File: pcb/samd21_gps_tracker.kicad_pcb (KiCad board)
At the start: 4 copper layers, 99 x 38.5 mm, 95 parts, among them J1 JTAG_SWD_6, J2 01x04, J3 U.FL-R-SMT, J4 SIM_Card, J5 USB_C_Receptacle_USB2.0, J6 U.FL-R-SMT, J7 C7244, Q1 2N7002, Q2 2N7002, Q3 2N7002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

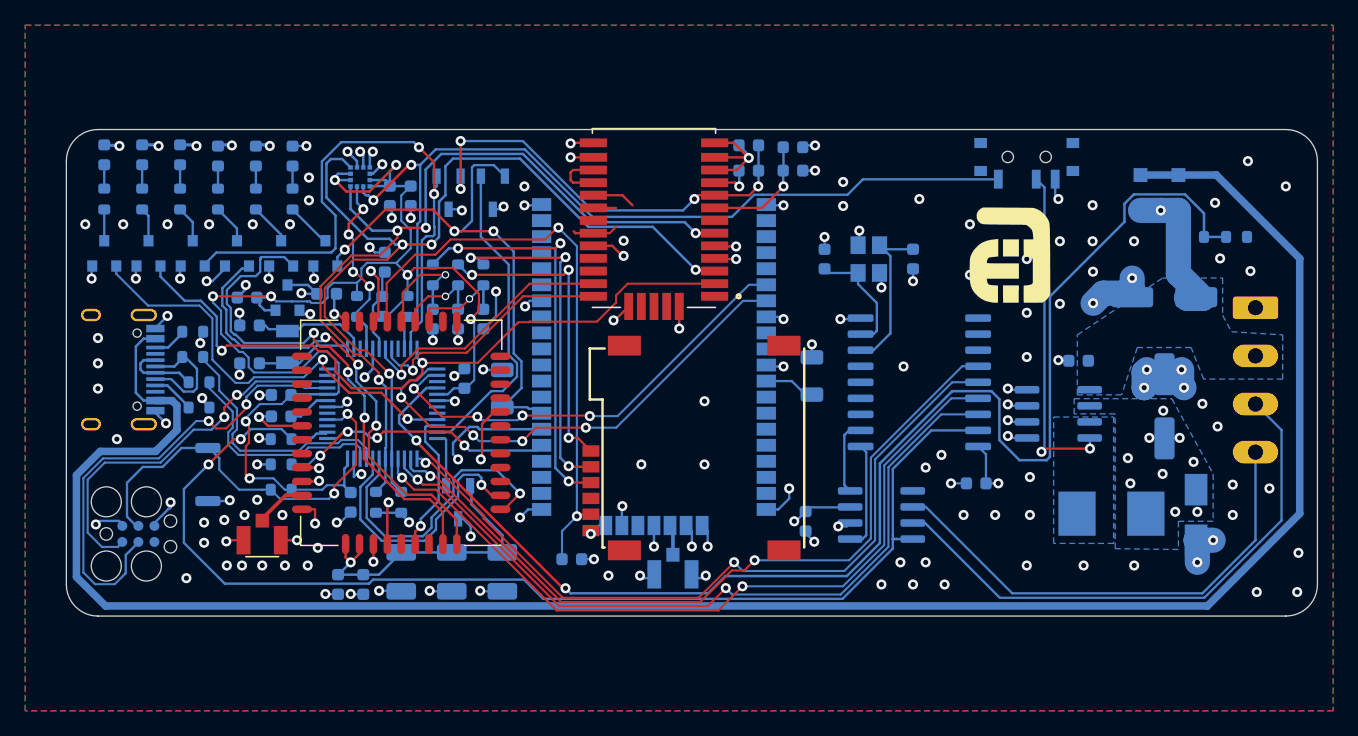
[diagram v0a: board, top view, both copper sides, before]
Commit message: REV 1 - WIP
Fixed D3, it was the wrong way around
Fixed Q6, Q7, Q8, D and S were the wrong way around
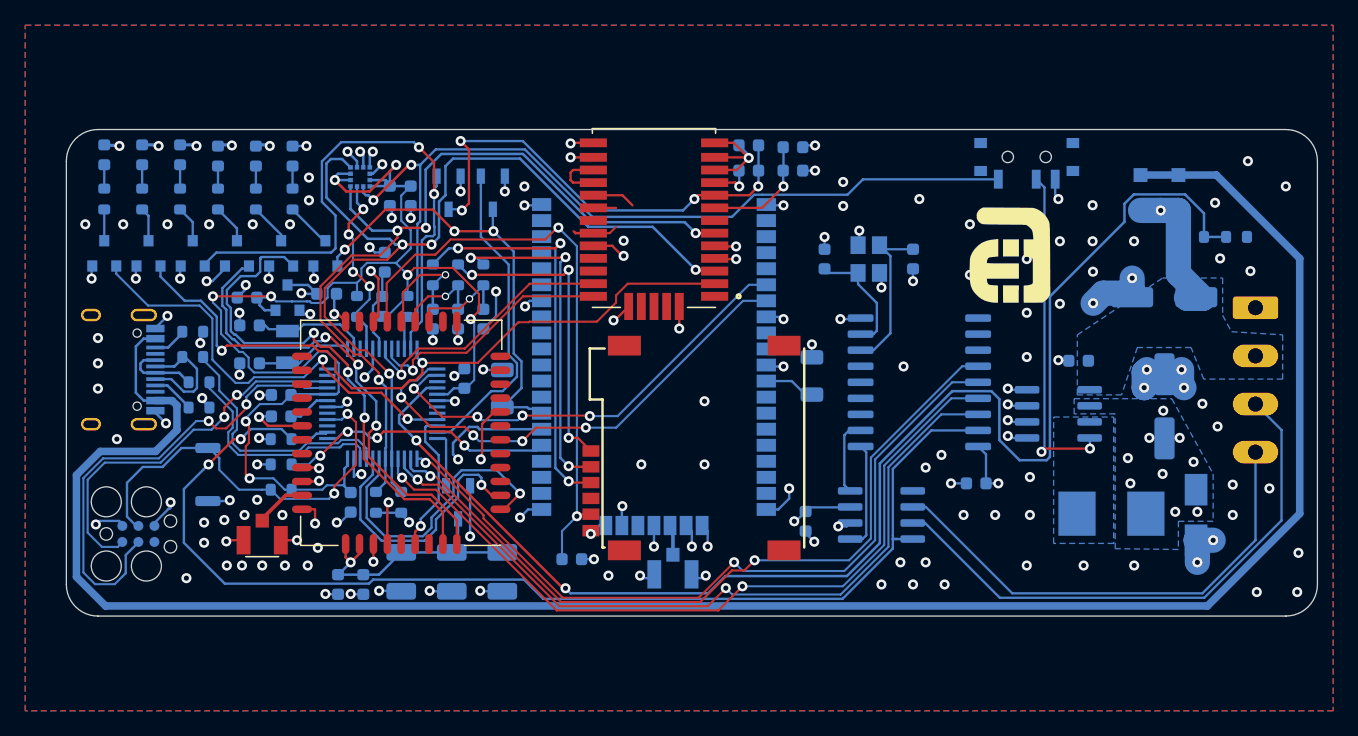
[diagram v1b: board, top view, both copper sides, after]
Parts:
- turned D3 to 270 degrees
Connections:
- D3 pad 1: GND -> +3V3
- D3 pad 2: +3V3 -> GND
- Q6 pad 2: LoRa_VCC -> +3V3
- Q6 pad 3: +3V3 -> LoRa_VCC
- Q7 pad 2: Net-(C15-Pad1) -> +3V3
- Q7 pad 3: +3V3 -> Net-(C15-Pad1)
- Q8 pad 2: Net-(C26-Pad1) -> +3V3
- Q8 pad 3: +3V3 -> Net-(C26-Pad1)
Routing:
- net LoRa_VCC: track 47.5 -> 40.2 mm
- net Net-(C26-Pad1): track 24.7 -> 21.0 mm
- net +3V3: track 37.4 -> 39.8 mm
- net Net-(C15-Pad1): track 34.7 -> 37.0 mm
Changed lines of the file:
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@@
     (thickness 1.6)
     (drawings 18)
-    (tracks 1464)
+    (tracks 1456)
     (zones 0)
     (modules 95)
@@
   )
   (setup
-    (last_trace_width 0.167)
+    (last_trace_width 0.187)
     (user_trace_width 0.187)
     (user_trace_width 0.2)
@@
   )
   (module Diode_SMD:D_SMA (layer B.Cu)
-    (at 227.9 68 90)
+    (at 227.9 68 270)
     (descr "Diode SMA (DO-214AC)")
     (tags "Diode SMA (DO-214AC)")
@@
       (effects (font (size 1 1) (thickness 0.15)) (justify mirror))
     )
-    (pad 1 smd rect (at -2 0 90) (size 2.5 1.8) (layers B.Cu B.Paste B.Mask)
-      (net 1 GND))
-    (pad 2 smd rect (at 2 0 90) (size 2.5 1.8) (layers B.Cu B.Paste B.Mask)
+    (pad 1 smd rect (at -2 0 270) (size 2.5 1.8) (layers B.Cu B.Paste B.Mask)
       (net 4 +3V3))
+    (pad 2 smd rect (at 2 0 270) (size 2.5 1.8) (layers B.Cu B.Paste B.Mask)
+      (net 1 GND))
     (model ${KISYS3DMOD}/Diode_SMD.3dshapes/D_SMA.wrl
       (at (xyz 0 0 0))
@@
     )
     (pad 3 smd rect (at 1.31 0 270) (size 1.22 0.65) (layers B.Cu B.Paste B.Mask)
-      (net 4 +3V3))
-    (pad 2 smd rect (at -1.31 -0.95 270) (size 1.22 0.65) (layers B.Cu B.Paste B.Mask)
       (net 10 LoRa_VCC))
+    (pad 2 smd rect (at -1.31 -0.95 270) (size 1.22 0.65) (layers B.Cu B.Paste B.Mask)
+      (net 4 +3V3))
     (pad 1 smd rect (at -1.31 0.95 270) (size 1.22 0.65) (layers B.Cu B.Paste B.Mask)
       (net 42 LoRa_ON))
@@
       (net 39 GPS_ON))
     (pad 2 smd rect (at -1.31 -0.95 270) (size 1.22 0.65) (layers B.Cu B.Paste B.Mask)
-      (net 11 "Net-(C15-Pad1)"))
-    (pad 3 smd rect (at 1.31 0 270) (size 1.22 0.65) (layers B.Cu B.Paste B.Mask)
       (net 4 +3V3))
+    (pad 3 smd rect (at 1.31 0 270) (size 1.22 0.65) (layers B.Cu B.Paste B.Mask)
+      (net 11 "Net-(C15-Pad1)"))
     (model ${KISYS3DMOD}/Package_TO_SOT_SMD.3dshapes/TSOT-23.wrl
       (at (xyz 0 0 0))
@@
       (net 43 SIM_ON))
     (pad 2 smd rect (at -1.31 -0.95 270) (size 1.22 0.65) (layers B.Cu B.Paste B.Mask)
-      (net 16 "Net-(C26-Pad1)"))
-    (pad 3 smd rect (at 1.31 0 270) (size 1.22 0.65) (layers B.Cu B.Paste B.Mask)
       (net 4 +3V3))
+    (pad 3 smd rect (at 1.31 0 270) (size 1.22 0.65) (layers B.Cu B.Paste B.Mask)
+      (net 16 "Net-(C26-Pad1)"))
     (model ${KISYS3DMOD}/Package_TO_SOT_SMD.3dshapes/TSOT-23.wrl
       (at (xyz 0 0 0))
@@
       (rotate (xyz 0 0 0))
     )
+    (model ${KISYS3DMOD}/Crystal.3dshapes/Crystal_SMD_0603-4Pin_6.0x3.5mm.step
+      (at (xyz 0 0 0))
+      (scale (xyz 0.5 0.5 1))
+      (rotate (xyz 0 0 0))
+    )
   )
   (module Crystal:Crystal_SMD_3225-4Pin_3.2x2.5mm (layer B.Cu)
@@
   (gr_line (start 237.5 40) (end 237.5 73.5) (layer Edge.Cuts) (width 0.05))
   (gr_line (start 141 37.5) (end 235 37.5) (layer Edge.Cuts) (width 0.05))
+  (via (at 169.7 42.4) (size 0.8) (drill 0.4) (layers F.Cu B.Cu) (net 4))
   (via (at 174.75 43.5) (size 0.8) (drill 0.4) (layers F.Cu B.Cu) (net 1))
   (segment (start 176.045 43.5) (end 176.11 43.435) (width 0.187) (layer B.Cu) (net 1) (status 30))
@@
   (via (at 229.6 61) (size 0.8) (drill 0.4) (layers F.Cu B.Cu) (net 1))
   (via (at 230.8 65.6) (size 0.8) (drill 0.4) (layers F.Cu B.Cu) (net 1))
-  (via (at 230.8 68) (size 0.8) (drill 0.4) (layers F.Cu B.Cu) (net 1))
+  (via (at 230.8 68) (size 0.8) (drill 0.4) (layers F.Cu B.Cu) (net 4))
   (via (at 223 72) (size 0.8) (drill 0.4) (layers F.Cu B.Cu) (net 1))
   (via (at 219 72) (size 0.8) (drill 0.4) (layers F.Cu B.Cu) (net 1))
@@
   (via (at 227.7 63.8) (size 0.8) (drill 0.4) (layers F.Cu B.Cu) (net 4))
   (via (at 225.25 64.75) (size 0.8) (drill 0.4) (layers F.Cu B.Cu) (net 4))
-  (via (at 226.25 67.75) (size 0.8) (drill 0.4) (layers F.Cu B.Cu) (net 4))
+  (via (at 226.25 67.75) (size 0.8) (drill 0.4) (layers F.Cu B.Cu) (net 1))
   (via (at 228 67.75) (size 0.8) (drill 0.4) (layers F.Cu B.Cu) (net 4))
   (via (at 226.6 61.9) (size 0.8) (drill 0.4) (layers F.Cu B.Cu) (net 4))
@@
   (segment (start 153.83949 62) (end 153.75 61.91051) (width 0.187) (layer B.Cu) (net 4))
   (segment (start 154.675 62) (end 153.83949 62) (width 0.187) (layer B.Cu) (net 4) (status 10))
-  (segment (start 172.25 43.81) (end 172.89 43.81) (width 0.187) (layer B.Cu) (net 4) (status 10))
-  (segment (start 172.89 43.81) (end 173.1 43.6) (width 0.187) (layer B.Cu) (net 4))
-  (via (at 173.1 43.6) (size 0.8) (drill 0.4) (layers F.Cu B.Cu) (net 4))
   (segment (start 148.7125 38.7125) (end 148.8 38.8) (width 0.25) (layer B.Cu) (net 4))
   (segment (start 147.5 38.7125) (end 148.7125 38.7125) (width 0.25) (layer B.Cu) (net 4) (status 10))
@@
   (segment (start 197 67.725) (end 196.225 68.5) (width 0.187) (layer B.Cu) (net 4) (status 10))
   (via (at 196.1 68.5) (size 0.8) (drill 0.4) (layers F.Cu B.Cu) (net 4))
-  (via (at 169.8 43.9) (size 0.8) (drill 0.4) (layers F.Cu B.Cu) (net 4))
-  (segment (start 168.75 43.81) (end 169.71 43.81) (width 0.187) (layer B.Cu) (net 4) (status 10))
-  (segment (start 169.71 43.81) (end 169.8 43.9) (width 0.187) (layer B.Cu) (net 4))
-  (via (at 170.5 69.7) (size 0.8) (drill 0.4) (layers F.Cu B.Cu) (net 4))
-  (segment (start 169.91 68.31) (end 170.5 68.9) (width 0.187) (layer B.Cu) (net 4))
-  (segment (start 170.5 68.9) (end 170.5 69.7) (width 0.187) (layer B.Cu) (net 4))
-  (segment (start 169.5 68.31) (end 169.91 68.31) (width 0.187) (layer B.Cu) (net 4) (status 10))
+  (segment (start 169.7 42.4) (end 169.7 41.19) (width 0.187) (layer B.Cu) (net 4))
+  (via (at 173.2 42.4) (size 0.8) (drill 0.4) (layers F.Cu B.Cu) (net 4))
+  (segment (start 173.2 42.4) (end 173.2 41.19) (width 0.187) (layer B.Cu) (net 4))
+  (via (at 170.45 69.7) (size 0.8) (drill 0.4) (layers F.Cu B.Cu) (net 4))
+  (segment (start 170.45 65.69) (end 170.45 69.7) (width 0.187) (layer B.Cu) (net 4))
+  (via (at 169.8 43.9) (size 0.8) (drill 0.4) (layers F.Cu B.Cu) (net 11))
+  (segment (start 168.75 43.81) (end 169.71 43.81) (width 0.187) (layer B.Cu) (net 11) (status 10))
+  (segment (start 169.71 43.81) (end 169.8 43.9) (width 0.187) (layer B.Cu) (net 11))
   (segment (start 157.05 60.2) (end 156.275 60.2) (width 0.2) (layer B.Cu) (net 5) (status 20))
   (segment (start 158.3 58.95) (end 157.05 60.2) (width 0.2) (layer B.Cu) (net 5))
@@
   (segment (start 169.211276 45.54949) (end 167.501285 43.839499) (width 0.187) (layer F.Cu) (net 10))
   (segment (start 167.501285 43.839499) (end 163.741156 43.839499) (width 0.187) (layer F.Cu) (net 10))
-  (segment (start 170.6 44.726451) (end 169.776961 45.54949) (width 0.187) (layer B.Cu) (net 10))
-  (segment (start 170.6 40.486098) (end 170.6 44.726451) (width 0.187) (layer B.Cu) (net 10))
-  (segment (start 169.776961 45.54949) (end 169.211276 45.54949) (width 0.187) (layer B.Cu) (net 10))
-  (segment (start 170.766599 40.319499) (end 170.6 40.486098) (width 0.187) (layer B.Cu) (net 10))
-  (segment (start 172.329499 40.319499) (end 170.766599 40.319499) (width 0.187) (layer B.Cu) (net 10))
-  (segment (start 173.2 41.19) (end 172.329499 40.319499) (width 0.187) (layer B.Cu) (net 10) (status 10))
   (segment (start 175.765 59.6) (end 176.11 59.945) (width 0.187) (layer B.Cu) (net 10) (status 30))
   (segment (start 174.975 59.475) (end 175.1 59.6) (width 0.187) (layer B.Cu) (net 10))
   (segment (start 175.1 59.6) (end 175.765 59.6) (width 0.187) (layer B.Cu) (net 10) (status 20))
   (segment (start 173 59.475) (end 174.975 59.475) (width 0.187) (layer B.Cu) (net 10) (status 10))
+  (segment (start 172.25 45.49949) (end 172.3 45.54949) (width 0.187) (layer B.Cu) (net 10))
+  (segment (start 172.25 43.81) (end 172.25 45.49949) (width 0.187) (layer B.Cu) (net 10))
   (via (at 193.25 42) (size 0.8) (drill 0.4) (layers F.Cu B.Cu) (net 11))
   (segment (start 193.275 38.75) (end 193.275 41.975) (width 0.187) (layer B.Cu) (net 11) (status 10))
@@
   (segment (start 188.5 42.7) (end 188.2 43) (width 0.187) (layer F.Cu) (net 11))
   (segment (start 189.8 42.7) (end 188.5 42.7) (width 0.187) (layer F.Cu) (net 11) (status 10))
-  (segment (start 169.700619 38.411968) (end 169.700619 42.199379) (width 0.2) (layer F.Cu) (net 11))
-  (segment (start 169.7 41.19) (end 169.7 42.19876) (width 0.2) (layer B.Cu) (net 11) (status 10))
-  (segment (start 169.7 42.19876) (end 169.700619 42.199379) (width 0.2) (layer B.Cu) (net 11))
-  (via (at 169.700619 42.199379) (size 0.8) (drill 0.4) (layers F.Cu B.Cu) (net 11))
   (segment (start 187.3 43.9) (end 188.2 43) (width 0.187) (layer B.Cu) (net 11))
   (segment (start 180.110486 43.9) (end 187.3 43.9) (width 0.187) (layer B.Cu) (net 11))
   (segment (start 174.622454 38.411968) (end 180.110486 43.9) (width 0.187) (layer B.Cu) (net 11))
   (segment (start 169.700619 38.411968) (end 174.622454 38.411968) (width 0.187) (layer B.Cu) (net 11))
+  (segment (start 170.360501 43.339499) (end 170.360501 39.07185) (width 0.187) (layer F.Cu) (net 11))
+  (segment (start 170.360501 39.07185) (end 169.700619 38.411968) (width 0.187) (layer F.Cu) (net 11))
+  (segment (start 169.8 43.9) (end 170.360501 43.339499) (width 0.187) (layer F.Cu) (net 11))
   (segment (start 171.5 51.725) (end 171.5 49.825) (width 0.2) (layer B.Cu) (net 12) (status 30))
   (segment (start 169.65051 51.64949) (end 170.4 50.9) (width 0.167) (layer F.Cu) (net 12))
@@
   (segment (start 165 70.9625) (end 163.2375 72.725) (width 0.2) (layer B.Cu) (net 16) (status 10))
   (segment (start 163.2375 72.725) (end 162 72.725) (width 0.2) (layer B.Cu) (net 16) (status 20))
-  (segment (start 173 69.6) (end 173 70.9625) (width 0.2) (layer B.Cu) (net 16) (status 20))
-  (segment (start 170.56 67.16) (end 173 69.6) (width 0.2) (layer B.Cu) (net 16))
-  (segment (start 170.56 65.69) (end 170.56 67.16) (width 0.2) (layer B.Cu) (net 16) (status 10))
+  (segment (start 169.5 68.31) (end 169.5 70.85) (width 0.187) (layer B.Cu) (net 16))
   (segment (start 141.5 40.3) (end 141.6 40.2) (width 0.25) (layer B.Cu) (net 17) (status 30))
   (segment (start 141.6 40.2) (end 141.4 40.2) (width 0.25) (layer B.Cu) (net 17) (status 30))

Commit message: WIP
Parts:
- moved SW2 0.40 mm to (214.5, 39.6)
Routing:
- net LoRa_VCC: track 40.2 -> 60.6 mm, vias 3 -> 5
- net ~EN: track 26.7 -> 27.3 mm
- net GND: track 186.4 -> 186.9 mm

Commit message: WIP
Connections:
- net ~EN renamed ~{EN}
- net ~Reset renamed ~{Reset}
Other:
- net class Default removed
